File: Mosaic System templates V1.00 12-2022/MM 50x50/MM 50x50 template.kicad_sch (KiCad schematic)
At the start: 21 parts, among them J1 Conn_01x04, J2 INPUT, J3 CLK_INPUT, J4 OUTPUT, SW1 SPDT, SW2 SPST, U1 Opamp_Dual

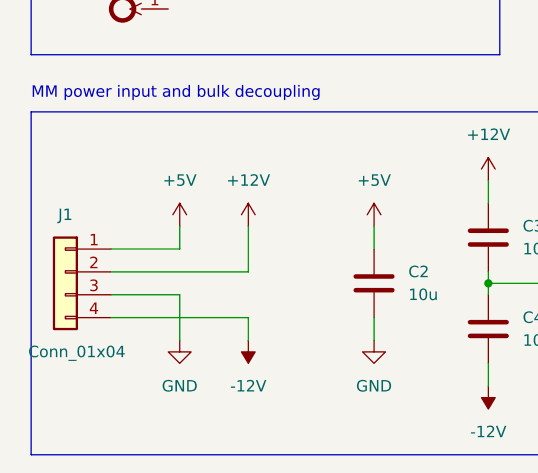
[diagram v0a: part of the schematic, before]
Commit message: V1.1
Clean up of some redundant footprints and added the correct polygons for the keepout area of the corners.
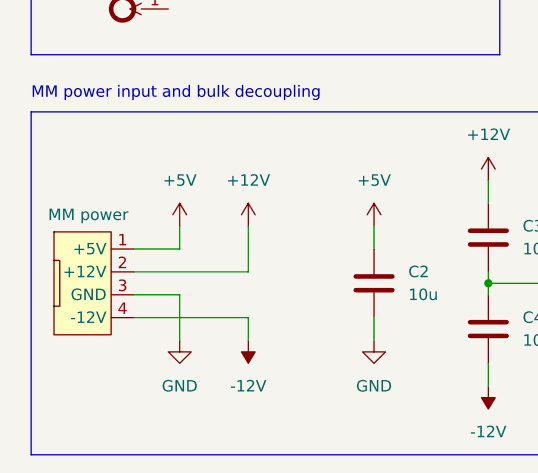
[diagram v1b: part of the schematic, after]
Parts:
- removed J1: Conn_01x04, 0-MM:JST_B4B-PH-SM4-TB_LF_SN_0, symbol Connector_Generic:Conn_01x04
- added J5: MM power, 0-MM:MM power JST, symbol 0-MM:MM power
- C2, C3, C4, C5: footprint Capacitor_SMD:C_0805_2012Metric -> (none)
- D2: footprint 0-MM:LED 0805 reverse mount -> (none)
- SW2: footprint 0-MM:12X12MM_THT_TACT -> (none)
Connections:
- net +12V: now also J5.2 (+12V)
- net +5V: now also J5.1 (+5V)
- net -12V: now also J5.4 (-12V)
- net GND: now also J5.3 (GND)
